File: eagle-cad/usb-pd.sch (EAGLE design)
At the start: 44 parts, among them Q1 CERAMIC_RESONATOR_SMD6M00G53Z, Q2 FDN352A, U1 ATMEGA328-AU

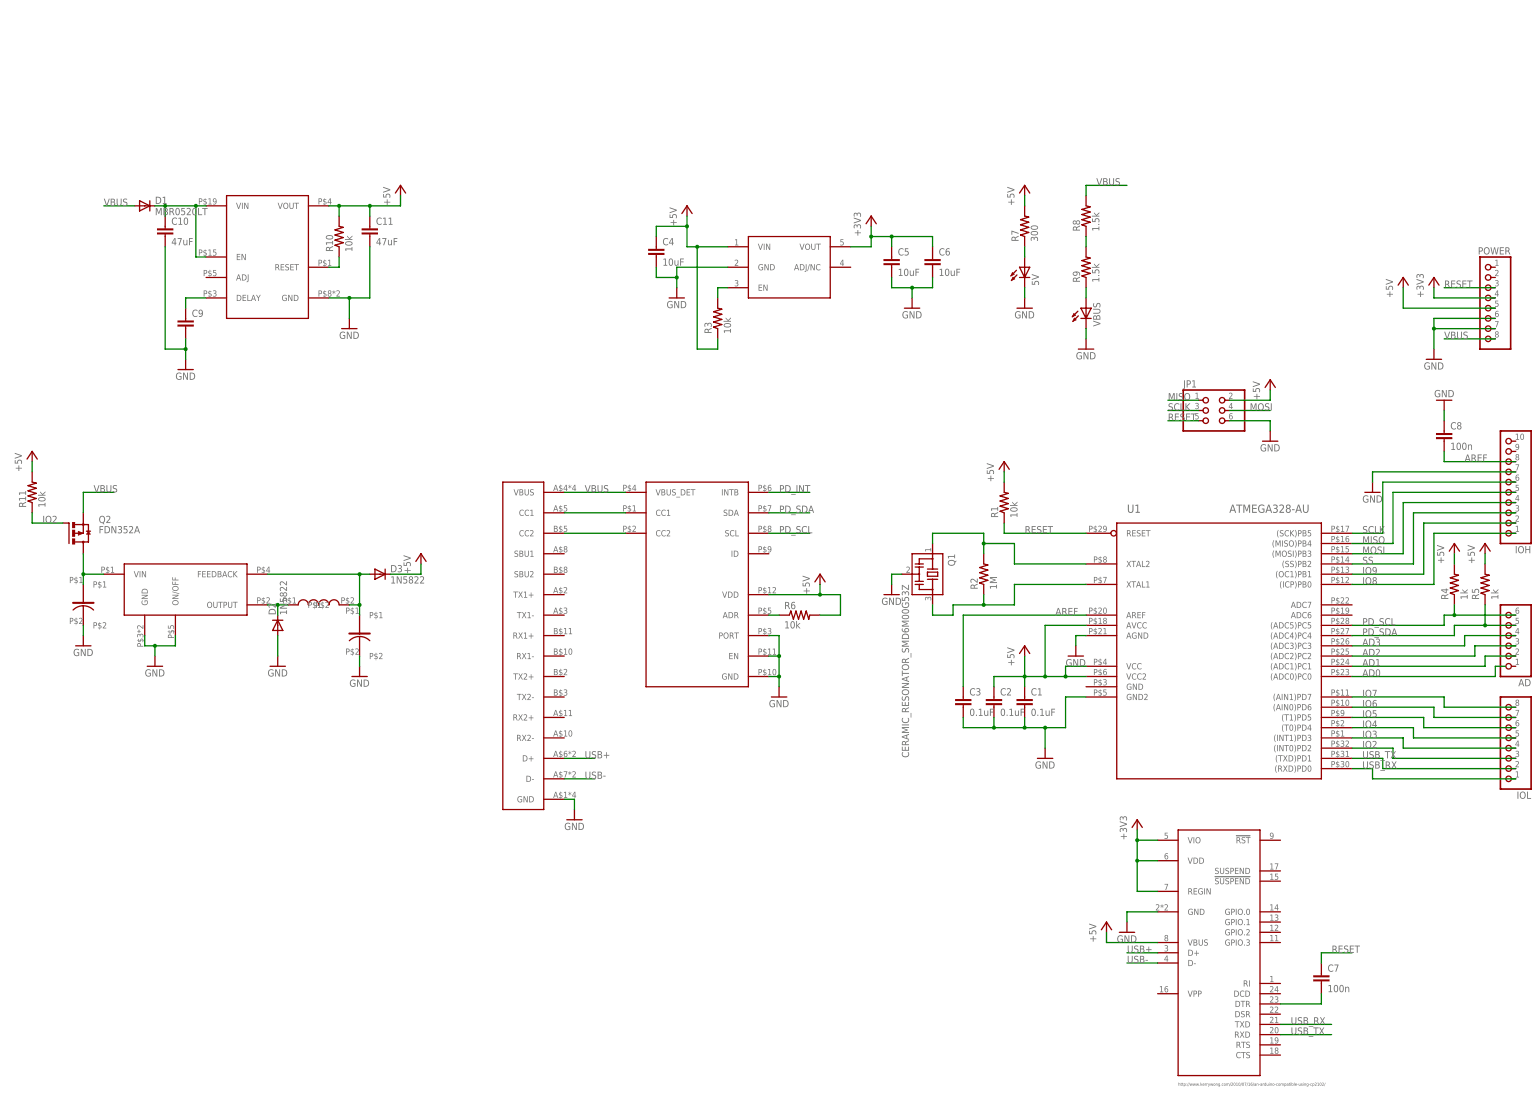
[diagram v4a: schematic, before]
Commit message: Started researching proper capacitors, modified parts to have name and value on schematic
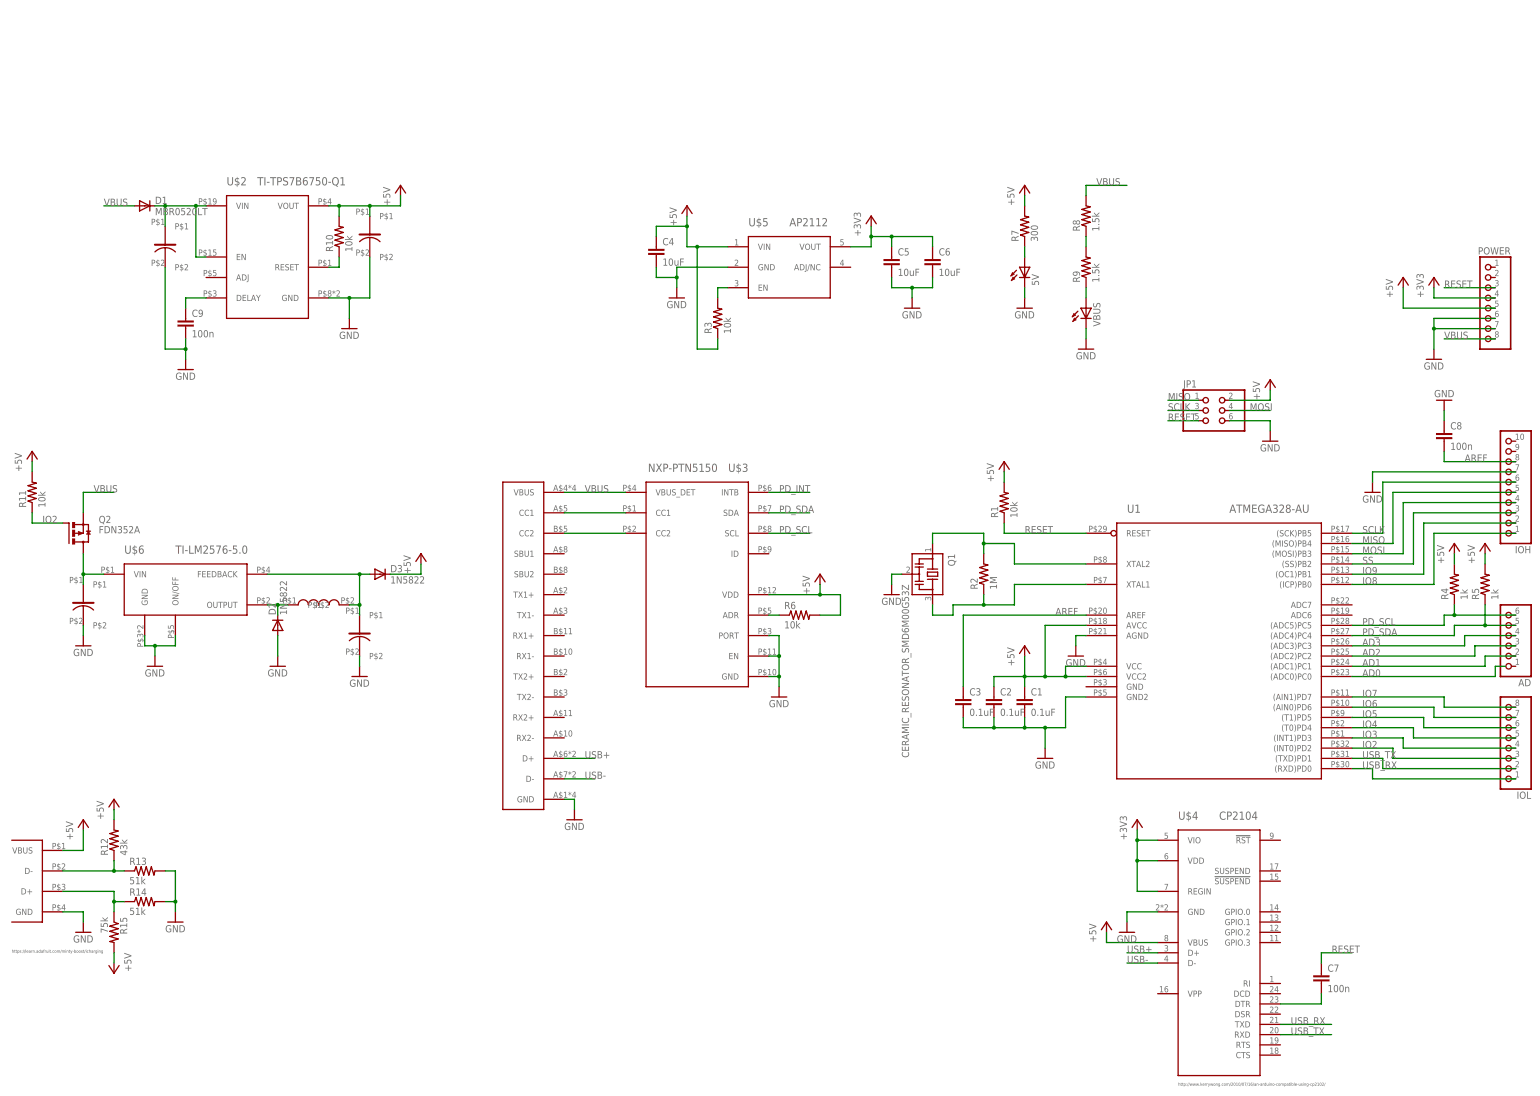
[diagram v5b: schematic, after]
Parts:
- removed C10, C11: 47uF, rcl:C-EUC0805
- added R12: 43k, rcl:R-US_R0402
- added R13, R14: 51k, rcl:R-US_R0402
- added R15: 75k, rcl:R-US_R0402
- added U$10: WURTH-865080543009-47uF, usb-pd:WURTH-865080543009
- added U$11: WURTH-865090543005-22uF, usb-pd:WURTH-865090543005
- added U$9: UE27AC54100, usb-pd:UE27AC54100
- C1, C2, C3, C8: device rcl:C-EUC0805 -> rcl:C-EUC0402
- C9: value (none) -> 100n
- R1, R2, R4, R5, R6, R7, R8, R9: device rcl:R-US_R0805 -> rcl:R-US_R0402
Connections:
- new net N$17: R12.1, R13.1, U$9.D-
- new net N$18: R14.1, R15.1, U$9.D+
- net +5V: now also R12.2, R15.2, U$11.P$1, U$9.VBUS; no longer C11.1
- net GND: now also R13.2, R14.2, U$10.P$2, U$11.P$2, U$9.GND; no longer C10.2, C11.2
- net N$40: now also U$10.P$1; no longer C10.1
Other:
- note added: "https://learn.adafruit.com/minty-boost/icharging"

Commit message: Finished placement, started routing
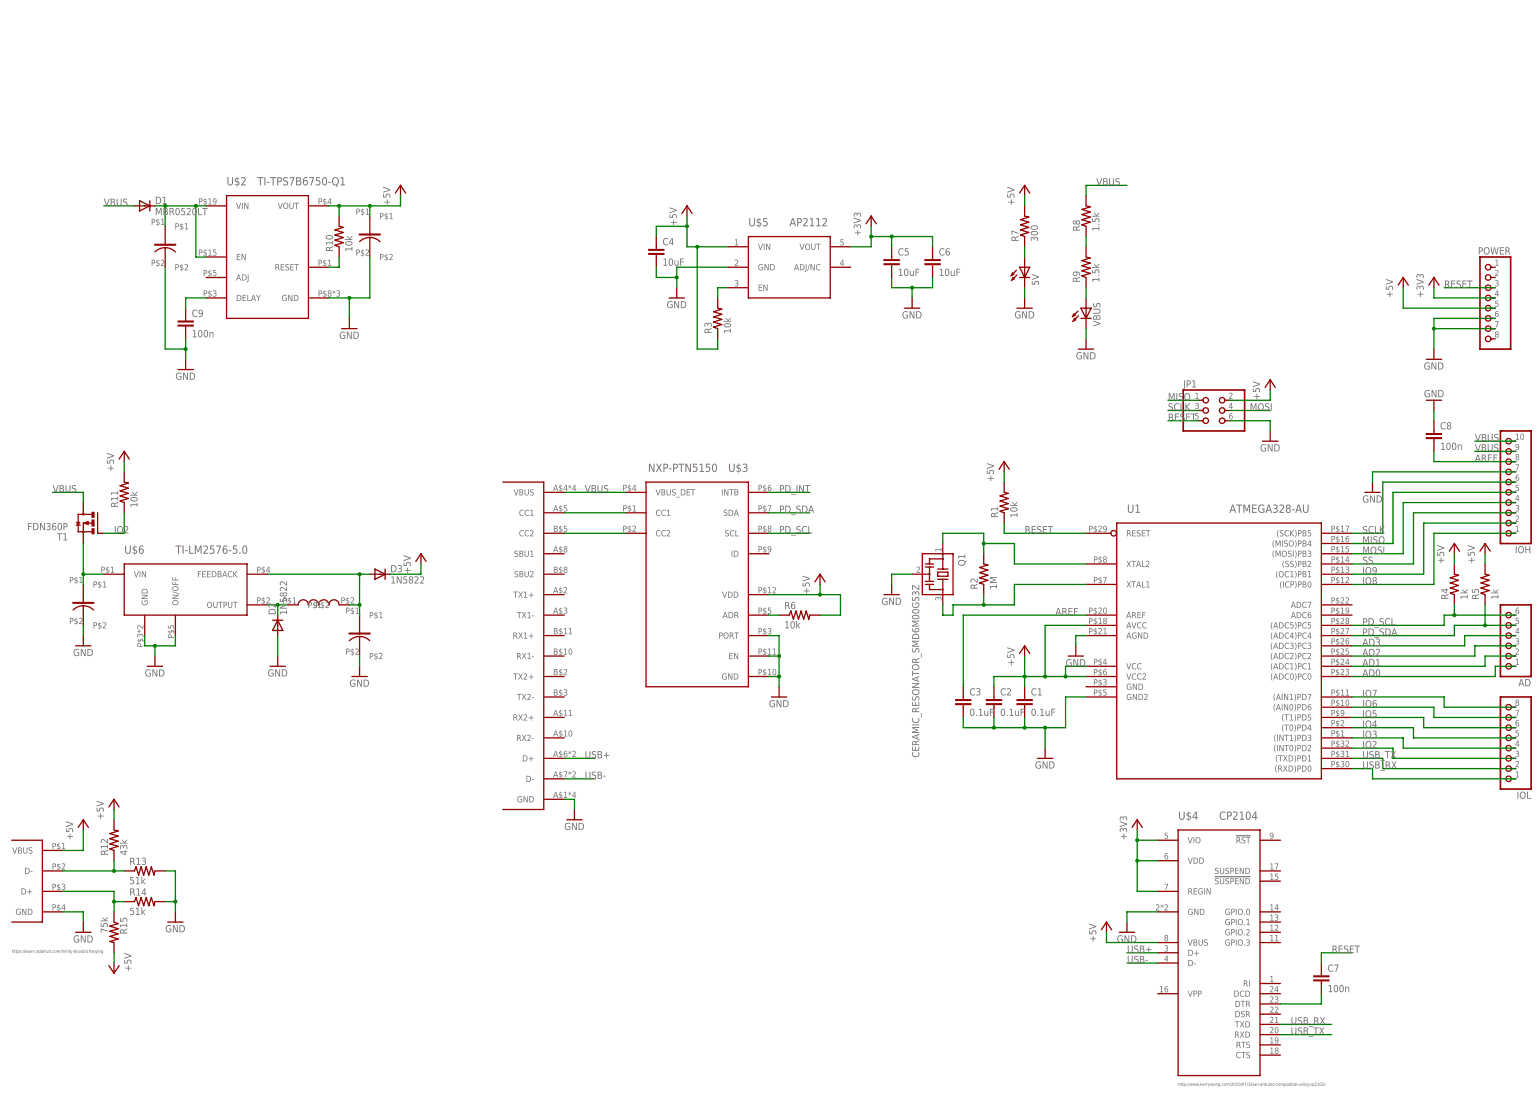
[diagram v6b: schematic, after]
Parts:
- removed Q2: FDN352A, transistor-power:FDN360P
- added T1: FDN360P, transistor-power:FDN360P
- C7: device rcl:C-EUC0805 -> rcl:C-EUC0402
- C9: device rcl:C-EUC0805 -> rcl:C-EUC0603
- R11, R3: device rcl:R-US_R0805 -> rcl:R-US_R0402
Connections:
- net AD0: now also AD.1
- net IO2: now also T1.G; no longer Q2.G
- net N$1: now also T1.S; no longer Q2.D
- net VBUS: now also IOH.10, IOH.9, T1.D; no longer POWER.8, Q2.S
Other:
- moved on the sheet: C8, Q1, R11

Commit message: Entire-board-routed, rev-1. This is going to need a lot of revisions.
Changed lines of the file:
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@@
 <instance part="C9" gate="G$1" x="-93.98" y="121.92"/>
 <instance part="D1" gate="G$1" x="-104.14" y="149.86"/>
-<instance part="GND16" gate="1" x="215.9" y="111.76"/>
+<instance part="GND16" gate="1" x="215.9" y="114.3"/>
 <instance part="P+11" gate="1" x="208.28" y="132.08"/>
 <instance part="+3V3" gate="G$1" x="215.9" y="132.08"/>
@@
 <segment>
 <pinref part="GND16" gate="1" pin="GND"/>
-<wire x1="215.9" y1="114.3" x2="215.9" y2="119.38" width="0.1524" layer="91"/>
+<wire x1="215.9" y1="116.84" x2="215.9" y2="119.38" width="0.1524" layer="91"/>
 <wire x1="215.9" y1="119.38" x2="215.9" y2="121.92" width="0.1524" layer="91"/>
 <junction x="215.9" y="119.38"/>
@@
 <wire x1="195.58" y1="10.16" x2="200.66" y2="10.16" width="0.1524" layer="91"/>
 <wire x1="200.66" y1="10.16" x2="200.66" y2="7.62" width="0.1524" layer="91"/>
+<label x="198.12" y="10.16" size="1.778" layer="95"/>
 <pinref part="IOL" gate="A" pin="1"/>
 <wire x1="200.66" y1="7.62" x2="236.22" y2="7.62" width="0.1524" layer="91"/>
-<label x="198.12" y="10.16" size="1.778" layer="95"/>
 </segment>
 </net>
@@
 <wire x1="195.58" y1="12.7" x2="203.2" y2="12.7" width="0.1524" layer="91"/>
 <wire x1="203.2" y1="12.7" x2="203.2" y2="10.16" width="0.1524" layer="91"/>
+<label x="198.12" y="12.7" size="1.778" layer="95"/>
 <pinref part="IOL" gate="A" pin="2"/>
 <wire x1="203.2" y1="10.16" x2="236.22" y2="10.16" width="0.1524" layer="91"/>
-<label x="198.12" y="12.7" size="1.778" layer="95"/>
 </segment>
 </net>
@@
 <wire x1="195.58" y1="15.24" x2="205.74" y2="15.24" width="0.1524" layer="91"/>
 <wire x1="205.74" y1="15.24" x2="205.74" y2="12.7" width="0.1524" layer="91"/>
+<label x="198.12" y="15.24" size="1.778" layer="95"/>
 <pinref part="IOL" gate="A" pin="3"/>
 <wire x1="205.74" y1="12.7" x2="236.22" y2="12.7" width="0.1524" layer="91"/>
-<label x="198.12" y="15.24" size="1.778" layer="95"/>
 </segment>
 <segment>
@@
 <wire x1="195.58" y1="17.78" x2="208.28" y2="17.78" width="0.1524" layer="91"/>
 <wire x1="208.28" y1="17.78" x2="208.28" y2="15.24" width="0.1524" layer="91"/>
+<label x="198.12" y="17.78" size="1.778" layer="95"/>
 <pinref part="IOL" gate="A" pin="4"/>
 <wire x1="208.28" y1="15.24" x2="236.22" y2="15.24" width="0.1524" layer="91"/>
-<label x="198.12" y="17.78" size="1.778" layer="95"/>
 </segment>
 </net>
@@
 <wire x1="195.58" y1="20.32" x2="210.82" y2="20.32" width="0.1524" layer="91"/>
 <wire x1="210.82" y1="20.32" x2="210.82" y2="17.78" width="0.1524" layer="91"/>
+<label x="198.12" y="20.32" size="1.778" layer="95"/>
 <pinref part="IOL" gate="A" pin="5"/>
 <wire x1="210.82" y1="17.78" x2="236.22" y2="17.78" width="0.1524" layer="91"/>
-<label x="198.12" y="20.32" size="1.778" layer="95"/>
 </segment>
 </net>
@@
 <wire x1="195.58" y1="22.86" x2="213.36" y2="22.86" width="0.1524" layer="91"/>
 <wire x1="213.36" y1="22.86" x2="213.36" y2="20.32" width="0.1524" layer="91"/>
+<label x="198.12" y="22.86" size="1.778" layer="95"/>
 <pinref part="IOL" gate="A" pin="6"/>
 <wire x1="213.36" y1="20.32" x2="236.22" y2="20.32" width="0.1524" layer="91"/>
-<label x="198.12" y="22.86" size="1.778" layer="95"/>
 </segment>
 </net>
@@
 <wire x1="195.58" y1="25.4" x2="215.9" y2="25.4" width="0.1524" layer="91"/>
 <wire x1="215.9" y1="25.4" x2="215.9" y2="22.86" width="0.1524" layer="91"/>
+<label x="198.12" y="25.4" size="1.778" layer="95"/>
 <pinref part="IOL" gate="A" pin="7"/>
 <wire x1="215.9" y1="22.86" x2="236.22" y2="22.86" width="0.1524" layer="91"/>
-<label x="198.12" y="25.4" size="1.778" layer="95"/>
 </segment>
 </net>
@@
 <wire x1="195.58" y1="27.94" x2="218.44" y2="27.94" width="0.1524" layer="91"/>
 <wire x1="218.44" y1="27.94" x2="218.44" y2="25.4" width="0.1524" layer="91"/>
+<label x="198.12" y="27.94" size="1.778" layer="95"/>
 <pinref part="IOL" gate="A" pin="8"/>
 <wire x1="218.44" y1="25.4" x2="236.22" y2="25.4" width="0.1524" layer="91"/>
-<label x="198.12" y="27.94" size="1.778" layer="95"/>
-</segment>
-</net>
+</segment>
+</net>

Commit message: Added new USB-C port, going to look at four-layer boards to get better Osh Park hole tolerances and ton of space for power planes
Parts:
- removed U$11: WURTH-865090543005-22uF, usb-pd:WURTH-865090543005
- removed U$6: TI-LM2576-5.0, usb-pd:TI-LM2576-5.0
- removed U1: ATMEGA328-AU, usb-pd:ATMEGA328-AU
- added C11: AVE108M10G24T-F, usb-pd:AVE108M10G24T-F
- added J$1: TYPE-C-12401548E4, usb-pd:TYPE-C-12401548E4
- added J$2: UE27AC54100, usb-pd:UE27AC54100
- C13: value AVE108M10G24T-F -> WURTH-865090543005-22uF; device usb-pd:AVE108M10G24T-F -> usb-pd:WURTH-865090543005
- U$1: value TYPE-C-BR20-AK511 -> TI-LM2576-5.0; device usb-pd:TYPE-C-BR20-AK511 -> usb-pd:TI-LM2576-5.0
- U$9: value UE27AC54100 -> ATMEGA328-AU; device usb-pd:UE27AC54100 -> usb-pd:ATMEGA328-AU
- renumbered U$10 to C12, U$8 to C10
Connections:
- net +5V: now also C13.P$1, J$2.VBUS, U$9.AVCC, U$9.VCC, U$9.VCC2; no longer U$11.P$1, U$9.VBUS, U1.AVCC, U1.VCC, U1.VCC2
- net AD0: now also U$9.(ADC0)PC0; no longer U1.(ADC0)PC0
- net AD1: now also U$9.(ADC1)PC1; no longer U1.(ADC1)PC1
- net AD2: now also U$9.(ADC2)PC2; no longer U1.(ADC2)PC2
- net AD3: now also U$9.(ADC3)PC3; no longer U1.(ADC3)PC3
- net AREF: now also U$9.AREF; no longer U1.AREF
- net GND: now also C11.P$2, J$1.GND, J$2.GND, U$1.ON/OFF, U$9.AGND, U$9.GND2; no longer U$11.P$2, U$6.GND, U$6.ON/OFF, U$9.GND, U1.AGND, U1.GND2
- net IO2: now also U$9.(INT0)PD2; no longer U1.(INT0)PD2
- net IO3: now also U$9.(INT1)PD3; no longer U1.(INT1)PD3
- net IO4: now also U$9.(T0)PD4; no longer U1.(T0)PD4
- net IO5: now also U$9.(T1)PD5; no longer U1.(T1)PD5
- net IO6: now also U$9.(AIN0)PD6; no longer U1.(AIN0)PD6
- net IO7: now also U$9.(AIN1)PD7; no longer U1.(AIN1)PD7
- net IO8: now also U$9.(ICP)PB0; no longer U1.(ICP)PB0
- net IO9: now also U$9.(OC1)PB1; no longer U1.(OC1)PB1
- net MISO: now also U$9.(MISO)PB4; no longer U1.(MISO)PB4
- net MOSI: now also U$9.(MOSI)PB3; no longer U1.(MOSI)PB3
- net N$1: now also U$1.VIN; no longer U$6.VIN
- net N$15: now also C11.P$1, U$1.FEEDBACK; no longer C13.P$1, U$6.FEEDBACK
- net N$17: now also J$2.D-; no longer U$9.D-
- net N$18: now also J$2.D+; no longer U$9.D+
- net N$2: now also U$9.XTAL1; no longer U1.XTAL1
- net N$3: now also U$9.XTAL2; no longer U1.XTAL2
- net N$5: now also J$1.CC1; no longer U$1.CC1
- net N$6: now also J$1.CC2; no longer U$1.CC2
- net N$9: now also U$1.OUTPUT; no longer U$6.OUTPUT
- net PD_SCL: now also U$9.(ADC5)PC5; no longer U1.(ADC5)PC5
- net PD_SDA: now also U$9.(ADC4)PC4; no longer U1.(ADC4)PC4
- net RESET: now also U$9.RESET; no longer U1.RESET
- net SCLK: now also U$9.(SCK)PB5; no longer U1.(SCK)PB5
- net SS: now also U$9.(SS)PB2; no longer U1.(SS)PB2
- net USB+: now also J$1.D+; no longer U$1.D+
- net USB-: now also J$1.D-; no longer U$1.D-
- net USB_RX: now also U$9.(RXD)PD0; no longer U1.(RXD)PD0
- net USB_TX: now also U$9.(TXD)PD1; no longer U1.(TXD)PD1
- net VBUS: now also J$1.VBUS; no longer U$1.VBUS
